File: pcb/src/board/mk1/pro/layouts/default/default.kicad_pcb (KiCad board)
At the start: 2 copper layers, 0 parts

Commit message: pcb: add MCU to Wonkleboard mk.1 Pro
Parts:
- added C1: 100nF ±10%, Samsung_Electro_Mechanics_CL05B104KO5NNNC:C0402, F.Cu at (20.0, 0.00)
- added C10: 100nF ±10%, Samsung_Electro_Mechanics_CL05B104KO5NNNC:C0402, F.Cu at (20.0, -90.0)
- added C11: 100nF ±10%, Samsung_Electro_Mechanics_CL05B104KO5NNNC:C0402, F.Cu at (20.0, -100.0)
- added C12: 100nF ±10%, Samsung_Electro_Mechanics_CL05B104KO5NNNC:C0402, F.Cu at (20.0, -110.0)
- added C13: 20pF ±5%, FH_0402CG200J500NT:C0402, F.Cu at (20.0, -130.0)
- added C14: 20pF ±5%, FH_0402CG200J500NT:C0402, F.Cu at (20.0, -140.0)
- added C15: 2.2µF ±20%, Samsung_Electro_Mechanics_CL05A225MQ5NSNC:C0402, F.Cu at (20.0, -150.0)
- added C16: 2.2µF ±20%, Samsung_Electro_Mechanics_CL05A225MQ5NSNC:C0402, F.Cu at (20.0, -160.0)
- added C17: 1µF ±10%, Samsung_Electro_Mechanics_CL05A105KA5NQNC:C0402, F.Cu at (20.0, -170.0)
- added C18: 100nF ±10%, Samsung_Electro_Mechanics_CL05B104KO5NNNC:C0402, F.Cu at (20.0, -180.0)
- added C2: 100nF ±10%, Samsung_Electro_Mechanics_CL05B104KO5NNNC:C0402, F.Cu at (20.0, -10.0)
- added C3: 100nF ±10%, Samsung_Electro_Mechanics_CL05B104KO5NNNC:C0402, F.Cu at (20.0, -20.0)
- added C4: 100nF ±10%, Samsung_Electro_Mechanics_CL05B104KO5NNNC:C0402, F.Cu at (20.0, -30.0)
- added C5: 100nF ±10%, Samsung_Electro_Mechanics_CL05B104KO5NNNC:C0402, F.Cu at (20.0, -40.0)
- added C6: 100nF ±10%, Samsung_Electro_Mechanics_CL05B104KO5NNNC:C0402, F.Cu at (20.0, -50.0)
- added C7: 100nF ±10%, Samsung_Electro_Mechanics_CL05B104KO5NNNC:C0402, F.Cu at (20.0, -60.0)
- added C8: 100nF ±10%, Samsung_Electro_Mechanics_CL05B104KO5NNNC:C0402, F.Cu at (20.0, -70.0)
- added C9: 100nF ±10%, Samsung_Electro_Mechanics_CL05B104KO5NNNC:C0402, F.Cu at (20.0, -80.0)
- added R1: 1kΩ ±1%, UNI_ROYAL_0402WGF1001TCE:R0402, F.Cu at (20.0, -120.0)
- added U1: , STMicroelectronics_STM32F429IGT6:LQFP-176_L24.0-W24.0-P0.50-LS26.0-BL, F.Cu at (0.00, 0.00)
- added X1: , TAE_TAXM8M4RFDCET2T:CRYSTAL-SMD_4P-L3.2-W2.5-BL-2, F.Cu at (10.0, 0.00)

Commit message: pcb: add MUX and sensors to Wonkleboard mk.1 Pro
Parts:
- added U10: , PJSEMI_AH49HSC:SOT-23-3_L2.9-W1.6-P1.90-LS2.8-BR, F.Cu at (72.0, 0.00)
- added U100: , PJSEMI_AH49HSC:SOT-23-3_L2.9-W1.6-P1.90-LS2.8-BR, F.Cu at (882.0, 0.00)
- added U101: , PJSEMI_AH49HSC:SOT-23-3_L2.9-W1.6-P1.90-LS2.8-BR, F.Cu at (891.0, 0.00)
- added U102: , PJSEMI_AH49HSC:SOT-23-3_L2.9-W1.6-P1.90-LS2.8-BR, F.Cu at (900.0, 0.00)
- added U103: , PJSEMI_AH49HSC:SOT-23-3_L2.9-W1.6-P1.90-LS2.8-BR, F.Cu at (909.0, 0.00)
- added U104: , PJSEMI_AH49HSC:SOT-23-3_L2.9-W1.6-P1.90-LS2.8-BR, F.Cu at (918.0, 0.00)
- added U105: , PJSEMI_AH49HSC:SOT-23-3_L2.9-W1.6-P1.90-LS2.8-BR, F.Cu at (927.0, 0.00)
- added U106: , PJSEMI_AH49HSC:SOT-23-3_L2.9-W1.6-P1.90-LS2.8-BR, F.Cu at (936.0, 0.00)
- added U107: , PJSEMI_AH49HSC:SOT-23-3_L2.9-W1.6-P1.90-LS2.8-BR, F.Cu at (945.0, 0.00)
- added U108: , PJSEMI_AH49HSC:SOT-23-3_L2.9-W1.6-P1.90-LS2.8-BR, F.Cu at (954.0, 0.00)
- added U109: , PJSEMI_AH49HSC:SOT-23-3_L2.9-W1.6-P1.90-LS2.8-BR, F.Cu at (963.0, 0.00)
- added U11: , PJSEMI_AH49HSC:SOT-23-3_L2.9-W1.6-P1.90-LS2.8-BR, F.Cu at (81.0, 0.00)
- added U110: , Texas_Instruments_CD74HC4067SM96:SSOP-24_L8.1-W5.3-P0.65-LS7.8-BL, F.Cu at (972.0, 0.00)
- added U111: , PJSEMI_AH49HSC:SOT-23-3_L2.9-W1.6-P1.90-LS2.8-BR, F.Cu at (981.0, 0.00)
- added U112: , PJSEMI_AH49HSC:SOT-23-3_L2.9-W1.6-P1.90-LS2.8-BR, F.Cu at (990.0, 0.00)
- added U113: , PJSEMI_AH49HSC:SOT-23-3_L2.9-W1.6-P1.90-LS2.8-BR, F.Cu at (999.0, 0.00)
- added U114: , PJSEMI_AH49HSC:SOT-23-3_L2.9-W1.6-P1.90-LS2.8-BR, F.Cu at (1008.0, 0.00)
- added U115: , PJSEMI_AH49HSC:SOT-23-3_L2.9-W1.6-P1.90-LS2.8-BR, F.Cu at (1017.0, 0.00)
- added U116: , PJSEMI_AH49HSC:SOT-23-3_L2.9-W1.6-P1.90-LS2.8-BR, F.Cu at (1026.0, 0.00)
- added U117: , PJSEMI_AH49HSC:SOT-23-3_L2.9-W1.6-P1.90-LS2.8-BR, F.Cu at (1035.0, 0.00)
- added U118: , PJSEMI_AH49HSC:SOT-23-3_L2.9-W1.6-P1.90-LS2.8-BR, F.Cu at (1044.0, 0.00)
- added U119: , PJSEMI_AH49HSC:SOT-23-3_L2.9-W1.6-P1.90-LS2.8-BR, F.Cu at (1053.0, 0.00)
- added U12: , PJSEMI_AH49HSC:SOT-23-3_L2.9-W1.6-P1.90-LS2.8-BR, F.Cu at (90.0, 0.00)
- added U120: , PJSEMI_AH49HSC:SOT-23-3_L2.9-W1.6-P1.90-LS2.8-BR, F.Cu at (1062.0, 0.00)
- added U121: , PJSEMI_AH49HSC:SOT-23-3_L2.9-W1.6-P1.90-LS2.8-BR, F.Cu at (1071.0, 0.00)
- added U122: , Texas_Instruments_CD74HC4067SM96:SSOP-24_L8.1-W5.3-P0.65-LS7.8-BL, F.Cu at (1080.0, 0.00)
- added U123: , PJSEMI_AH49HSC:SOT-23-3_L2.9-W1.6-P1.90-LS2.8-BR, F.Cu at (1089.0, 0.00)
- added U124: , PJSEMI_AH49HSC:SOT-23-3_L2.9-W1.6-P1.90-LS2.8-BR, F.Cu at (1098.0, 0.00)
- added U125: , PJSEMI_AH49HSC:SOT-23-3_L2.9-W1.6-P1.90-LS2.8-BR, F.Cu at (1107.0, 0.00)
- added U126: , PJSEMI_AH49HSC:SOT-23-3_L2.9-W1.6-P1.90-LS2.8-BR, F.Cu at (1116.0, 0.00)
- added U127: , PJSEMI_AH49HSC:SOT-23-3_L2.9-W1.6-P1.90-LS2.8-BR, F.Cu at (1125.0, 0.00)
- added U128: , PJSEMI_AH49HSC:SOT-23-3_L2.9-W1.6-P1.90-LS2.8-BR, F.Cu at (1134.0, 0.00)
- added U129: , PJSEMI_AH49HSC:SOT-23-3_L2.9-W1.6-P1.90-LS2.8-BR, F.Cu at (1143.0, 0.00)
- added U13: , PJSEMI_AH49HSC:SOT-23-3_L2.9-W1.6-P1.90-LS2.8-BR, F.Cu at (99.0, 0.00)
- added U130: , PJSEMI_AH49HSC:SOT-23-3_L2.9-W1.6-P1.90-LS2.8-BR, F.Cu at (1152.0, 0.00)
- added U131: , PJSEMI_AH49HSC:SOT-23-3_L2.9-W1.6-P1.90-LS2.8-BR, F.Cu at (1161.0, 0.00)
- added U132: , PJSEMI_AH49HSC:SOT-23-3_L2.9-W1.6-P1.90-LS2.8-BR, F.Cu at (1170.0, 0.00)
- added U133: , PJSEMI_AH49HSC:SOT-23-3_L2.9-W1.6-P1.90-LS2.8-BR, F.Cu at (1179.0, 0.00)
- added U134: , Texas_Instruments_CD74HC4067SM96:SSOP-24_L8.1-W5.3-P0.65-LS7.8-BL, F.Cu at (1188.0, 0.00)
- added U135: , PJSEMI_AH49HSC:SOT-23-3_L2.9-W1.6-P1.90-LS2.8-BR, F.Cu at (1197.0, 0.00)
- added U136: , PJSEMI_AH49HSC:SOT-23-3_L2.9-W1.6-P1.90-LS2.8-BR, F.Cu at (1206.0, 0.00)
- added U137: , PJSEMI_AH49HSC:SOT-23-3_L2.9-W1.6-P1.90-LS2.8-BR, F.Cu at (1215.0, 0.00)
- added U138: , PJSEMI_AH49HSC:SOT-23-3_L2.9-W1.6-P1.90-LS2.8-BR, F.Cu at (1224.0, 0.00)
- added U139: , PJSEMI_AH49HSC:SOT-23-3_L2.9-W1.6-P1.90-LS2.8-BR, F.Cu at (1233.0, 0.00)
- added U14: , Texas_Instruments_CD74HC4067SM96:SSOP-24_L8.1-W5.3-P0.65-LS7.8-BL, F.Cu at (108.0, 0.00)
- added U140: , PJSEMI_AH49HSC:SOT-23-3_L2.9-W1.6-P1.90-LS2.8-BR, F.Cu at (1242.0, 0.00)
- added U141: , PJSEMI_AH49HSC:SOT-23-3_L2.9-W1.6-P1.90-LS2.8-BR, F.Cu at (1251.0, 0.00)
- added U142: , PJSEMI_AH49HSC:SOT-23-3_L2.9-W1.6-P1.90-LS2.8-BR, F.Cu at (1260.0, 0.00)
- added U143: , PJSEMI_AH49HSC:SOT-23-3_L2.9-W1.6-P1.90-LS2.8-BR, F.Cu at (1269.0, 0.00)
- added U144: , PJSEMI_AH49HSC:SOT-23-3_L2.9-W1.6-P1.90-LS2.8-BR, F.Cu at (1278.0, 0.00)
- added U145: , PJSEMI_AH49HSC:SOT-23-3_L2.9-W1.6-P1.90-LS2.8-BR, F.Cu at (1287.0, 0.00)
- added U146: , Texas_Instruments_CD74HC4067SM96:SSOP-24_L8.1-W5.3-P0.65-LS7.8-BL, F.Cu at (1296.0, 0.00)
- added U147: , PJSEMI_AH49HSC:SOT-23-3_L2.9-W1.6-P1.90-LS2.8-BR, F.Cu at (1305.0, 0.00)
- added U148: , PJSEMI_AH49HSC:SOT-23-3_L2.9-W1.6-P1.90-LS2.8-BR, F.Cu at (1314.0, 0.00)
- added U149: , PJSEMI_AH49HSC:SOT-23-3_L2.9-W1.6-P1.90-LS2.8-BR, F.Cu at (1323.0, 0.00)
- added U15: , PJSEMI_AH49HSC:SOT-23-3_L2.9-W1.6-P1.90-LS2.8-BR, F.Cu at (117.0, 0.00)
- added U150: , PJSEMI_AH49HSC:SOT-23-3_L2.9-W1.6-P1.90-LS2.8-BR, F.Cu at (1332.0, 0.00)
- added U151: , PJSEMI_AH49HSC:SOT-23-3_L2.9-W1.6-P1.90-LS2.8-BR, F.Cu at (1341.0, 0.00)
- added U152: , PJSEMI_AH49HSC:SOT-23-3_L2.9-W1.6-P1.90-LS2.8-BR, F.Cu at (1350.0, 0.00)
- added U153: , PJSEMI_AH49HSC:SOT-23-3_L2.9-W1.6-P1.90-LS2.8-BR, F.Cu at (1359.0, 0.00)
- added U154: , PJSEMI_AH49HSC:SOT-23-3_L2.9-W1.6-P1.90-LS2.8-BR, F.Cu at (1368.0, 0.00)
- added U155: , PJSEMI_AH49HSC:SOT-23-3_L2.9-W1.6-P1.90-LS2.8-BR, F.Cu at (1377.0, 0.00)
- added U156: , PJSEMI_AH49HSC:SOT-23-3_L2.9-W1.6-P1.90-LS2.8-BR, F.Cu at (1386.0, 0.00)
- added U157: , PJSEMI_AH49HSC:SOT-23-3_L2.9-W1.6-P1.90-LS2.8-BR, F.Cu at (1395.0, 0.00)
- added U158: , Texas_Instruments_CD74HC4067SM96:SSOP-24_L8.1-W5.3-P0.65-LS7.8-BL, F.Cu at (1404.0, 0.00)
- added U159: , PJSEMI_AH49HSC:SOT-23-3_L2.9-W1.6-P1.90-LS2.8-BR, F.Cu at (1413.0, 0.00)
- added U16: , PJSEMI_AH49HSC:SOT-23-3_L2.9-W1.6-P1.90-LS2.8-BR, F.Cu at (126.0, 0.00)
- added U160: , PJSEMI_AH49HSC:SOT-23-3_L2.9-W1.6-P1.90-LS2.8-BR, F.Cu at (1422.0, 0.00)
- added U161: , PJSEMI_AH49HSC:SOT-23-3_L2.9-W1.6-P1.90-LS2.8-BR, F.Cu at (1431.0, 0.00)
- added U162: , PJSEMI_AH49HSC:SOT-23-3_L2.9-W1.6-P1.90-LS2.8-BR, F.Cu at (1440.0, 0.00)
- added U163: , PJSEMI_AH49HSC:SOT-23-3_L2.9-W1.6-P1.90-LS2.8-BR, F.Cu at (1449.0, 0.00)
- added U164: , PJSEMI_AH49HSC:SOT-23-3_L2.9-W1.6-P1.90-LS2.8-BR, F.Cu at (1458.0, 0.00)
- added U165: , PJSEMI_AH49HSC:SOT-23-3_L2.9-W1.6-P1.90-LS2.8-BR, F.Cu at (1467.0, 0.00)
- added U166: , PJSEMI_AH49HSC:SOT-23-3_L2.9-W1.6-P1.90-LS2.8-BR, F.Cu at (1476.0, 0.00)
- added U167: , PJSEMI_AH49HSC:SOT-23-3_L2.9-W1.6-P1.90-LS2.8-BR, F.Cu at (1485.0, 0.00)
- added U168: , PJSEMI_AH49HSC:SOT-23-3_L2.9-W1.6-P1.90-LS2.8-BR, F.Cu at (1494.0, 0.00)
- added U169: , PJSEMI_AH49HSC:SOT-23-3_L2.9-W1.6-P1.90-LS2.8-BR, F.Cu at (1503.0, 0.00)
- added U17: , PJSEMI_AH49HSC:SOT-23-3_L2.9-W1.6-P1.90-LS2.8-BR, F.Cu at (135.0, 0.00)
- added U170: , Texas_Instruments_CD74HC4067SM96:SSOP-24_L8.1-W5.3-P0.65-LS7.8-BL, F.Cu at (1512.0, 0.00)
- added U171: , PJSEMI_AH49HSC:SOT-23-3_L2.9-W1.6-P1.90-LS2.8-BR, F.Cu at (1521.0, 0.00)
- added U172: , PJSEMI_AH49HSC:SOT-23-3_L2.9-W1.6-P1.90-LS2.8-BR, F.Cu at (1530.0, 0.00)
- added U173: , PJSEMI_AH49HSC:SOT-23-3_L2.9-W1.6-P1.90-LS2.8-BR, F.Cu at (1539.0, 0.00)
- added U174: , PJSEMI_AH49HSC:SOT-23-3_L2.9-W1.6-P1.90-LS2.8-BR, F.Cu at (1548.0, 0.00)
- added U175: , PJSEMI_AH49HSC:SOT-23-3_L2.9-W1.6-P1.90-LS2.8-BR, F.Cu at (1557.0, 0.00)
- added U176: , PJSEMI_AH49HSC:SOT-23-3_L2.9-W1.6-P1.90-LS2.8-BR, F.Cu at (1566.0, 0.00)
- added U177: , PJSEMI_AH49HSC:SOT-23-3_L2.9-W1.6-P1.90-LS2.8-BR, F.Cu at (1575.0, 0.00)
- added U178: , PJSEMI_AH49HSC:SOT-23-3_L2.9-W1.6-P1.90-LS2.8-BR, F.Cu at (1584.0, 0.00)
- added U179: , PJSEMI_AH49HSC:SOT-23-3_L2.9-W1.6-P1.90-LS2.8-BR, F.Cu at (1593.0, 0.00)
- added U18: , PJSEMI_AH49HSC:SOT-23-3_L2.9-W1.6-P1.90-LS2.8-BR, F.Cu at (144.0, 0.00)
- added U180: , PJSEMI_AH49HSC:SOT-23-3_L2.9-W1.6-P1.90-LS2.8-BR, F.Cu at (1602.0, 0.00)
- added U181: , PJSEMI_AH49HSC:SOT-23-3_L2.9-W1.6-P1.90-LS2.8-BR, F.Cu at (1611.0, 0.00)
- added U182: , Texas_Instruments_CD74HC4067SM96:SSOP-24_L8.1-W5.3-P0.65-LS7.8-BL, F.Cu at (1620.0, 0.00)
- added U183: , PJSEMI_AH49HSC:SOT-23-3_L2.9-W1.6-P1.90-LS2.8-BR, F.Cu at (1629.0, 0.00)
- added U184: , PJSEMI_AH49HSC:SOT-23-3_L2.9-W1.6-P1.90-LS2.8-BR, F.Cu at (1638.0, 0.00)
- added U185: , PJSEMI_AH49HSC:SOT-23-3_L2.9-W1.6-P1.90-LS2.8-BR, F.Cu at (1647.0, 0.00)
- added U186: , PJSEMI_AH49HSC:SOT-23-3_L2.9-W1.6-P1.90-LS2.8-BR, F.Cu at (1656.0, 0.00)
- added U187: , PJSEMI_AH49HSC:SOT-23-3_L2.9-W1.6-P1.90-LS2.8-BR, F.Cu at (1665.0, 0.00)
- added U188: , PJSEMI_AH49HSC:SOT-23-3_L2.9-W1.6-P1.90-LS2.8-BR, F.Cu at (1674.0, 0.00)
- added U189: , PJSEMI_AH49HSC:SOT-23-3_L2.9-W1.6-P1.90-LS2.8-BR, F.Cu at (1683.0, 0.00)
- added U19: , PJSEMI_AH49HSC:SOT-23-3_L2.9-W1.6-P1.90-LS2.8-BR, F.Cu at (153.0, 0.00)
- added U190: , PJSEMI_AH49HSC:SOT-23-3_L2.9-W1.6-P1.90-LS2.8-BR, F.Cu at (1692.0, 0.00)
- added U191: , PJSEMI_AH49HSC:SOT-23-3_L2.9-W1.6-P1.90-LS2.8-BR, F.Cu at (1701.0, 0.00)
- added U192: , PJSEMI_AH49HSC:SOT-23-3_L2.9-W1.6-P1.90-LS2.8-BR, F.Cu at (1710.0, 0.00)
- added U193: , PJSEMI_AH49HSC:SOT-23-3_L2.9-W1.6-P1.90-LS2.8-BR, F.Cu at (1719.0, 0.00)
- added U194: , Texas_Instruments_CD74HC4067SM96:SSOP-24_L8.1-W5.3-P0.65-LS7.8-BL, F.Cu at (1728.0, 0.00)
- added U195: , PJSEMI_AH49HSC:SOT-23-3_L2.9-W1.6-P1.90-LS2.8-BR, F.Cu at (1737.0, 0.00)
- added U196: , PJSEMI_AH49HSC:SOT-23-3_L2.9-W1.6-P1.90-LS2.8-BR, F.Cu at (1746.0, 0.00)
- added U197: , PJSEMI_AH49HSC:SOT-23-3_L2.9-W1.6-P1.90-LS2.8-BR, F.Cu at (1755.0, 0.00)
- added U198: , PJSEMI_AH49HSC:SOT-23-3_L2.9-W1.6-P1.90-LS2.8-BR, F.Cu at (1764.0, 0.00)
- added U199: , PJSEMI_AH49HSC:SOT-23-3_L2.9-W1.6-P1.90-LS2.8-BR, F.Cu at (1773.0, 0.00)
- added U2: , Texas_Instruments_CD74HC4067SM96:SSOP-24_L8.1-W5.3-P0.65-LS7.8-BL, F.Cu at (0.00, 0.00)
- added U20: , PJSEMI_AH49HSC:SOT-23-3_L2.9-W1.6-P1.90-LS2.8-BR, F.Cu at (162.0, 0.00)
- added U200: , PJSEMI_AH49HSC:SOT-23-3_L2.9-W1.6-P1.90-LS2.8-BR, F.Cu at (1782.0, 0.00)
- added U201: , PJSEMI_AH49HSC:SOT-23-3_L2.9-W1.6-P1.90-LS2.8-BR, F.Cu at (1791.0, 0.00)
- added U202: , PJSEMI_AH49HSC:SOT-23-3_L2.9-W1.6-P1.90-LS2.8-BR, F.Cu at (1800.0, 0.00)
- added U203: , PJSEMI_AH49HSC:SOT-23-3_L2.9-W1.6-P1.90-LS2.8-BR, F.Cu at (1809.0, 0.00)
- added U204: , PJSEMI_AH49HSC:SOT-23-3_L2.9-W1.6-P1.90-LS2.8-BR, F.Cu at (1818.0, 0.00)
- added U205: , PJSEMI_AH49HSC:SOT-23-3_L2.9-W1.6-P1.90-LS2.8-BR, F.Cu at (1827.0, 0.00)
- added U206: , Texas_Instruments_CD74HC4067SM96:SSOP-24_L8.1-W5.3-P0.65-LS7.8-BL, F.Cu at (1836.0, 0.00)
- added U207: , PJSEMI_AH49HSC:SOT-23-3_L2.9-W1.6-P1.90-LS2.8-BR, F.Cu at (1845.0, 0.00)
- added U208: , PJSEMI_AH49HSC:SOT-23-3_L2.9-W1.6-P1.90-LS2.8-BR, F.Cu at (1854.0, 0.00)
- added U209: , PJSEMI_AH49HSC:SOT-23-3_L2.9-W1.6-P1.90-LS2.8-BR, F.Cu at (1863.0, 0.00)
- added U21: , PJSEMI_AH49HSC:SOT-23-3_L2.9-W1.6-P1.90-LS2.8-BR, F.Cu at (171.0, 0.00)
- added U210: , PJSEMI_AH49HSC:SOT-23-3_L2.9-W1.6-P1.90-LS2.8-BR, F.Cu at (1872.0, 0.00)
- added U211: , PJSEMI_AH49HSC:SOT-23-3_L2.9-W1.6-P1.90-LS2.8-BR, F.Cu at (1881.0, 0.00)
- added U212: , PJSEMI_AH49HSC:SOT-23-3_L2.9-W1.6-P1.90-LS2.8-BR, F.Cu at (1890.0, 0.00)
- added U213: , PJSEMI_AH49HSC:SOT-23-3_L2.9-W1.6-P1.90-LS2.8-BR, F.Cu at (1899.0, 0.00)
- added U214: , PJSEMI_AH49HSC:SOT-23-3_L2.9-W1.6-P1.90-LS2.8-BR, F.Cu at (1908.0, 0.00)
- added U215: , PJSEMI_AH49HSC:SOT-23-3_L2.9-W1.6-P1.90-LS2.8-BR, F.Cu at (1917.0, 0.00)
- added U216: , PJSEMI_AH49HSC:SOT-23-3_L2.9-W1.6-P1.90-LS2.8-BR, F.Cu at (1926.0, 0.00)
- added U217: , PJSEMI_AH49HSC:SOT-23-3_L2.9-W1.6-P1.90-LS2.8-BR, F.Cu at (1935.0, 0.00)
- added U218: , Texas_Instruments_CD74HC4067SM96:SSOP-24_L8.1-W5.3-P0.65-LS7.8-BL, F.Cu at (1944.0, 0.00)
- added U219: , PJSEMI_AH49HSC:SOT-23-3_L2.9-W1.6-P1.90-LS2.8-BR, F.Cu at (1953.0, 0.00)
- added U22: , PJSEMI_AH49HSC:SOT-23-3_L2.9-W1.6-P1.90-LS2.8-BR, F.Cu at (180.0, 0.00)
- added U220: , PJSEMI_AH49HSC:SOT-23-3_L2.9-W1.6-P1.90-LS2.8-BR, F.Cu at (1962.0, 0.00)
- added U221: , PJSEMI_AH49HSC:SOT-23-3_L2.9-W1.6-P1.90-LS2.8-BR, F.Cu at (1971.0, 0.00)
- added U222: , PJSEMI_AH49HSC:SOT-23-3_L2.9-W1.6-P1.90-LS2.8-BR, F.Cu at (1980.0, 0.00)
- added U223: , PJSEMI_AH49HSC:SOT-23-3_L2.9-W1.6-P1.90-LS2.8-BR, F.Cu at (1989.0, 0.00)
- added U224: , PJSEMI_AH49HSC:SOT-23-3_L2.9-W1.6-P1.90-LS2.8-BR, F.Cu at (1998.0, 0.00)
- added U225: , PJSEMI_AH49HSC:SOT-23-3_L2.9-W1.6-P1.90-LS2.8-BR, F.Cu at (2007.0, 0.00)
- added U226: , PJSEMI_AH49HSC:SOT-23-3_L2.9-W1.6-P1.90-LS2.8-BR, F.Cu at (2016.0, 0.00)
- added U227: , PJSEMI_AH49HSC:SOT-23-3_L2.9-W1.6-P1.90-LS2.8-BR, F.Cu at (2025.0, 0.00)
- added U228: , PJSEMI_AH49HSC:SOT-23-3_L2.9-W1.6-P1.90-LS2.8-BR, F.Cu at (2034.0, 0.00)
- added U229: , PJSEMI_AH49HSC:SOT-23-3_L2.9-W1.6-P1.90-LS2.8-BR, F.Cu at (2043.0, 0.00)
- added U23: , PJSEMI_AH49HSC:SOT-23-3_L2.9-W1.6-P1.90-LS2.8-BR, F.Cu at (189.0, 0.00)
- added U24: , PJSEMI_AH49HSC:SOT-23-3_L2.9-W1.6-P1.90-LS2.8-BR, F.Cu at (198.0, 0.00)
- added U25: , PJSEMI_AH49HSC:SOT-23-3_L2.9-W1.6-P1.90-LS2.8-BR, F.Cu at (207.0, 0.00)
- added U26: , Texas_Instruments_CD74HC4067SM96:SSOP-24_L8.1-W5.3-P0.65-LS7.8-BL, F.Cu at (216.0, 0.00)
- added U27: , PJSEMI_AH49HSC:SOT-23-3_L2.9-W1.6-P1.90-LS2.8-BR, F.Cu at (225.0, 0.00)
- added U28: , PJSEMI_AH49HSC:SOT-23-3_L2.9-W1.6-P1.90-LS2.8-BR, F.Cu at (234.0, 0.00)
- added U29: , PJSEMI_AH49HSC:SOT-23-3_L2.9-W1.6-P1.90-LS2.8-BR, F.Cu at (243.0, 0.00)
- added U3: , PJSEMI_AH49HSC:SOT-23-3_L2.9-W1.6-P1.90-LS2.8-BR, F.Cu at (9.00, 0.00)
- added U30: , PJSEMI_AH49HSC:SOT-23-3_L2.9-W1.6-P1.90-LS2.8-BR, F.Cu at (252.0, 0.00)
- added U31: , PJSEMI_AH49HSC:SOT-23-3_L2.9-W1.6-P1.90-LS2.8-BR, F.Cu at (261.0, 0.00)
- added U32: , PJSEMI_AH49HSC:SOT-23-3_L2.9-W1.6-P1.90-LS2.8-BR, F.Cu at (270.0, 0.00)
- added U33: , PJSEMI_AH49HSC:SOT-23-3_L2.9-W1.6-P1.90-LS2.8-BR, F.Cu at (279.0, 0.00)
- added U34: , PJSEMI_AH49HSC:SOT-23-3_L2.9-W1.6-P1.90-LS2.8-BR, F.Cu at (288.0, 0.00)
- added U35: , PJSEMI_AH49HSC:SOT-23-3_L2.9-W1.6-P1.90-LS2.8-BR, F.Cu at (297.0, 0.00)
- added U36: , PJSEMI_AH49HSC:SOT-23-3_L2.9-W1.6-P1.90-LS2.8-BR, F.Cu at (306.0, 0.00)
- added U37: , PJSEMI_AH49HSC:SOT-23-3_L2.9-W1.6-P1.90-LS2.8-BR, F.Cu at (315.0, 0.00)
- added U38: , Texas_Instruments_CD74HC4067SM96:SSOP-24_L8.1-W5.3-P0.65-LS7.8-BL, F.Cu at (324.0, 0.00)
- added U39: , PJSEMI_AH49HSC:SOT-23-3_L2.9-W1.6-P1.90-LS2.8-BR, F.Cu at (333.0, 0.00)
- added U4: , PJSEMI_AH49HSC:SOT-23-3_L2.9-W1.6-P1.90-LS2.8-BR, F.Cu at (18.0, 0.00)
- added U40: , PJSEMI_AH49HSC:SOT-23-3_L2.9-W1.6-P1.90-LS2.8-BR, F.Cu at (342.0, 0.00)
- added U41: , PJSEMI_AH49HSC:SOT-23-3_L2.9-W1.6-P1.90-LS2.8-BR, F.Cu at (351.0, 0.00)
- added U42: , PJSEMI_AH49HSC:SOT-23-3_L2.9-W1.6-P1.90-LS2.8-BR, F.Cu at (360.0, 0.00)
- added U43: , PJSEMI_AH49HSC:SOT-23-3_L2.9-W1.6-P1.90-LS2.8-BR, F.Cu at (369.0, 0.00)
- added U44: , PJSEMI_AH49HSC:SOT-23-3_L2.9-W1.6-P1.90-LS2.8-BR, F.Cu at (378.0, 0.00)
- added U45: , PJSEMI_AH49HSC:SOT-23-3_L2.9-W1.6-P1.90-LS2.8-BR, F.Cu at (387.0, 0.00)
- added U46: , PJSEMI_AH49HSC:SOT-23-3_L2.9-W1.6-P1.90-LS2.8-BR, F.Cu at (396.0, 0.00)
- added U47: , PJSEMI_AH49HSC:SOT-23-3_L2.9-W1.6-P1.90-LS2.8-BR, F.Cu at (405.0, 0.00)
- added U48: , PJSEMI_AH49HSC:SOT-23-3_L2.9-W1.6-P1.90-LS2.8-BR, F.Cu at (414.0, 0.00)
- added U49: , PJSEMI_AH49HSC:SOT-23-3_L2.9-W1.6-P1.90-LS2.8-BR, F.Cu at (423.0, 0.00)
- added U5: , PJSEMI_AH49HSC:SOT-23-3_L2.9-W1.6-P1.90-LS2.8-BR, F.Cu at (27.0, 0.00)
- added U50: , Texas_Instruments_CD74HC4067SM96:SSOP-24_L8.1-W5.3-P0.65-LS7.8-BL, F.Cu at (432.0, 0.00)
- added U51: , PJSEMI_AH49HSC:SOT-23-3_L2.9-W1.6-P1.90-LS2.8-BR, F.Cu at (441.0, 0.00)
- added U52: , PJSEMI_AH49HSC:SOT-23-3_L2.9-W1.6-P1.90-LS2.8-BR, F.Cu at (450.0, 0.00)
- added U53: , PJSEMI_AH49HSC:SOT-23-3_L2.9-W1.6-P1.90-LS2.8-BR, F.Cu at (459.0, 0.00)
- added U54: , PJSEMI_AH49HSC:SOT-23-3_L2.9-W1.6-P1.90-LS2.8-BR, F.Cu at (468.0, 0.00)
- added U55: , PJSEMI_AH49HSC:SOT-23-3_L2.9-W1.6-P1.90-LS2.8-BR, F.Cu at (477.0, 0.00)
- added U56: , PJSEMI_AH49HSC:SOT-23-3_L2.9-W1.6-P1.90-LS2.8-BR, F.Cu at (486.0, 0.00)
- added U57: , PJSEMI_AH49HSC:SOT-23-3_L2.9-W1.6-P1.90-LS2.8-BR, F.Cu at (495.0, 0.00)
- added U58: , PJSEMI_AH49HSC:SOT-23-3_L2.9-W1.6-P1.90-LS2.8-BR, F.Cu at (504.0, 0.00)
- added U59: , PJSEMI_AH49HSC:SOT-23-3_L2.9-W1.6-P1.90-LS2.8-BR, F.Cu at (513.0, 0.00)
- added U6: , PJSEMI_AH49HSC:SOT-23-3_L2.9-W1.6-P1.90-LS2.8-BR, F.Cu at (36.0, 0.00)
- added U60: , PJSEMI_AH49HSC:SOT-23-3_L2.9-W1.6-P1.90-LS2.8-BR, F.Cu at (522.0, 0.00)
- added U61: , PJSEMI_AH49HSC:SOT-23-3_L2.9-W1.6-P1.90-LS2.8-BR, F.Cu at (531.0, 0.00)
- added U62: , Texas_Instruments_CD74HC4067SM96:SSOP-24_L8.1-W5.3-P0.65-LS7.8-BL, F.Cu at (540.0, 0.00)
- added U63: , PJSEMI_AH49HSC:SOT-23-3_L2.9-W1.6-P1.90-LS2.8-BR, F.Cu at (549.0, 0.00)
- added U64: , PJSEMI_AH49HSC:SOT-23-3_L2.9-W1.6-P1.90-LS2.8-BR, F.Cu at (558.0, 0.00)
- added U65: , PJSEMI_AH49HSC:SOT-23-3_L2.9-W1.6-P1.90-LS2.8-BR, F.Cu at (567.0, 0.00)
- added U66: , PJSEMI_AH49HSC:SOT-23-3_L2.9-W1.6-P1.90-LS2.8-BR, F.Cu at (576.0, 0.00)
- added U67: , PJSEMI_AH49HSC:SOT-23-3_L2.9-W1.6-P1.90-LS2.8-BR, F.Cu at (585.0, 0.00)
- added U68: , PJSEMI_AH49HSC:SOT-23-3_L2.9-W1.6-P1.90-LS2.8-BR, F.Cu at (594.0, 0.00)
- added U69: , PJSEMI_AH49HSC:SOT-23-3_L2.9-W1.6-P1.90-LS2.8-BR, F.Cu at (603.0, 0.00)
- added U7: , PJSEMI_AH49HSC:SOT-23-3_L2.9-W1.6-P1.90-LS2.8-BR, F.Cu at (45.0, 0.00)
- added U70: , PJSEMI_AH49HSC:SOT-23-3_L2.9-W1.6-P1.90-LS2.8-BR, F.Cu at (612.0, 0.00)
- added U71: , PJSEMI_AH49HSC:SOT-23-3_L2.9-W1.6-P1.90-LS2.8-BR, F.Cu at (621.0, 0.00)
- added U72: , PJSEMI_AH49HSC:SOT-23-3_L2.9-W1.6-P1.90-LS2.8-BR, F.Cu at (630.0, 0.00)
- added U73: , PJSEMI_AH49HSC:SOT-23-3_L2.9-W1.6-P1.90-LS2.8-BR, F.Cu at (639.0, 0.00)
- added U74: , Texas_Instruments_CD74HC4067SM96:SSOP-24_L8.1-W5.3-P0.65-LS7.8-BL, F.Cu at (648.0, 0.00)
- added U75: , PJSEMI_AH49HSC:SOT-23-3_L2.9-W1.6-P1.90-LS2.8-BR, F.Cu at (657.0, 0.00)
- added U76: , PJSEMI_AH49HSC:SOT-23-3_L2.9-W1.6-P1.90-LS2.8-BR, F.Cu at (666.0, 0.00)
- added U77: , PJSEMI_AH49HSC:SOT-23-3_L2.9-W1.6-P1.90-LS2.8-BR, F.Cu at (675.0, 0.00)
- added U78: , PJSEMI_AH49HSC:SOT-23-3_L2.9-W1.6-P1.90-LS2.8-BR, F.Cu at (684.0, 0.00)
- added U79: , PJSEMI_AH49HSC:SOT-23-3_L2.9-W1.6-P1.90-LS2.8-BR, F.Cu at (693.0, 0.00)
- added U8: , PJSEMI_AH49HSC:SOT-23-3_L2.9-W1.6-P1.90-LS2.8-BR, F.Cu at (54.0, 0.00)
- added U80: , PJSEMI_AH49HSC:SOT-23-3_L2.9-W1.6-P1.90-LS2.8-BR, F.Cu at (702.0, 0.00)
- added U81: , PJSEMI_AH49HSC:SOT-23-3_L2.9-W1.6-P1.90-LS2.8-BR, F.Cu at (711.0, 0.00)
- added U82: , PJSEMI_AH49HSC:SOT-23-3_L2.9-W1.6-P1.90-LS2.8-BR, F.Cu at (720.0, 0.00)
- added U83: , PJSEMI_AH49HSC:SOT-23-3_L2.9-W1.6-P1.90-LS2.8-BR, F.Cu at (729.0, 0.00)
- added U84: , PJSEMI_AH49HSC:SOT-23-3_L2.9-W1.6-P1.90-LS2.8-BR, F.Cu at (738.0, 0.00)
- added U85: , PJSEMI_AH49HSC:SOT-23-3_L2.9-W1.6-P1.90-LS2.8-BR, F.Cu at (747.0, 0.00)
- added U86: , Texas_Instruments_CD74HC4067SM96:SSOP-24_L8.1-W5.3-P0.65-LS7.8-BL, F.Cu at (756.0, 0.00)
- added U87: , PJSEMI_AH49HSC:SOT-23-3_L2.9-W1.6-P1.90-LS2.8-BR, F.Cu at (765.0, 0.00)
- added U88: , PJSEMI_AH49HSC:SOT-23-3_L2.9-W1.6-P1.90-LS2.8-BR, F.Cu at (774.0, 0.00)
- added U89: , PJSEMI_AH49HSC:SOT-23-3_L2.9-W1.6-P1.90-LS2.8-BR, F.Cu at (783.0, 0.00)
- added U9: , PJSEMI_AH49HSC:SOT-23-3_L2.9-W1.6-P1.90-LS2.8-BR, F.Cu at (63.0, 0.00)
- added U90: , PJSEMI_AH49HSC:SOT-23-3_L2.9-W1.6-P1.90-LS2.8-BR, F.Cu at (792.0, 0.00)
- added U91: , PJSEMI_AH49HSC:SOT-23-3_L2.9-W1.6-P1.90-LS2.8-BR, F.Cu at (801.0, 0.00)
- added U92: , PJSEMI_AH49HSC:SOT-23-3_L2.9-W1.6-P1.90-LS2.8-BR, F.Cu at (810.0, 0.00)
- added U93: , PJSEMI_AH49HSC:SOT-23-3_L2.9-W1.6-P1.90-LS2.8-BR, F.Cu at (819.0, 0.00)
- added U94: , PJSEMI_AH49HSC:SOT-23-3_L2.9-W1.6-P1.90-LS2.8-BR, F.Cu at (828.0, 0.00)
- added U95: , PJSEMI_AH49HSC:SOT-23-3_L2.9-W1.6-P1.90-LS2.8-BR, F.Cu at (837.0, 0.00)
- added U96: , PJSEMI_AH49HSC:SOT-23-3_L2.9-W1.6-P1.90-LS2.8-BR, F.Cu at (846.0, 0.00)
- added U97: , PJSEMI_AH49HSC:SOT-23-3_L2.9-W1.6-P1.90-LS2.8-BR, F.Cu at (855.0, 0.00)
- added U98: , Texas_Instruments_CD74HC4067SM96:SSOP-24_L8.1-W5.3-P0.65-LS7.8-BL, F.Cu at (864.0, 0.00)
- added U99: , PJSEMI_AH49HSC:SOT-23-3_L2.9-W1.6-P1.90-LS2.8-BR, F.Cu at (873.0, 0.00)
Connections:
- C1 pad 2: lv -> (no net)
- C10 pad 2: lv -> (no net)
- C11 pad 2: lv -> (no net)
- C12 pad 2: lv -> (no net)
- C13 pad 2: lv -> (no net)
- C14 pad 2: lv -> (no net)
- C15 pad 2: lv -> (no net)
- C16 pad 2: lv -> (no net)
- C17 pad 2: lv -> (no net)
- C18 pad 2: lv -> (no net)
- C2 pad 2: lv -> (no net)
- C3 pad 2: lv -> (no net)
- C4 pad 2: lv -> (no net)
- C5 pad 2: lv -> (no net)
- C6 pad 2: lv -> (no net)
- C7 pad 2: lv -> (no net)
- C8 pad 2: lv -> (no net)
- C9 pad 2: lv -> (no net)
- U1 pad 102: lv -> (no net)
- U1 pad 113: lv -> (no net)
- U1 pad 126: lv -> (no net)
- U1 pad 135: lv -> (no net)
- U1 pad 14: lv -> (no net)
- U1 pad 148: lv -> (no net)
- U1 pad 158: lv -> (no net)
- U1 pad 19: 19 -> gpio_f[3]-OUT
- U1 pad 2: 2 -> S3
- U1 pad 20: 20 -> gpio_f[4]-OUT
- U1 pad 21: 21 -> gpio_f[5]-OUT
- U1 pad 22: lv -> (no net)
- U1 pad 24: 24 -> gpio_f[6]-OUT
- U1 pad 25: 25 -> gpio_f[7]-OUT
- U1 pad 26: 26 -> gpio_f[8]-OUT
- U1 pad 27: 27 -> gpio_f[9]-OUT
- U1 pad 28: 28 -> gpio_f[10]-OUT
- U1 pad 3: 3 -> S2
- U1 pad 34: 34 -> gpio_c[2]-OUT
- U1 pad 35: 35 -> gpio_c[3]-OUT
- U1 pad 37: lv -> (no net)
- U1 pad 4: 4 -> S1
- U1 pad 41: 41 -> OUT
- U1 pad 42: 42 -> gpio_a[2]-OUT
- U1 pad 47: 47 -> gpio_a[3]-OUT
- U1 pad 5: 5 -> S0
- U1 pad 50: 50 -> gpio_a[4]-OUT
- U1 pad 52: 52 -> gpio_a[6]-OUT
- U1 pad 53: 53 -> gpio_a[7]-OUT
- U1 pad 54: 54 -> gpio_c[4]-OUT
- U1 pad 55: 55 -> gpio_c[5]-OUT
- U1 pad 61: lv -> (no net)
- U1 pad 71: lv -> (no net)
- U1 pad 90: lv -> (no net)
- X1 pad 2: lv -> (no net)
- X1 pad 4: lv -> (no net)

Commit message: pcb: oops forgot to commit this
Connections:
- C1 pad 2: (no net) -> lv
- C10 pad 2: (no net) -> lv
- C11 pad 2: (no net) -> lv
- C12 pad 2: (no net) -> lv
- C13 pad 2: (no net) -> lv
- C14 pad 2: (no net) -> lv
- C15 pad 2: (no net) -> lv
- C16 pad 2: (no net) -> lv
- C17 pad 2: (no net) -> lv
- C18 pad 2: (no net) -> lv
- C2 pad 2: (no net) -> lv
- C3 pad 2: (no net) -> lv
- C4 pad 2: (no net) -> lv
- C5 pad 2: (no net) -> lv
- C6 pad 2: (no net) -> lv
- C7 pad 2: (no net) -> lv
- C8 pad 2: (no net) -> lv
- C9 pad 2: (no net) -> lv
- U1 pad 102: (no net) -> lv
- U1 pad 113: (no net) -> lv
- U1 pad 126: (no net) -> lv
- U1 pad 135: (no net) -> lv
- U1 pad 14: (no net) -> lv
- U1 pad 148: (no net) -> lv
- U1 pad 158: (no net) -> lv
- U1 pad 22: (no net) -> lv
- U1 pad 37: (no net) -> lv
- U1 pad 61: (no net) -> lv
- U1 pad 71: (no net) -> lv
- U1 pad 90: (no net) -> lv
- U10 pad 3: (no net) -> lv
- U100 pad 3: (no net) -> lv
- U101 pad 3: (no net) -> lv
- U102 pad 3: (no net) -> lv
- U103 pad 3: (no net) -> lv
- U104 pad 3: (no net) -> lv
- U105 pad 3: (no net) -> lv
- U106 pad 3: (no net) -> lv
- U107 pad 3: (no net) -> lv
- U108 pad 3: (no net) -> lv
- U109 pad 3: (no net) -> lv
- U11 pad 3: (no net) -> lv
- U110 pad 12: (no net) -> lv
- U110 pad 15: (no net) -> lv
- U110 pad 16: (no net) -> lv
- U110 pad 17: (no net) -> lv
- U110 pad 18: (no net) -> lv
- U110 pad 19: (no net) -> lv
- U110 pad 20: (no net) -> lv
- U111 pad 3: (no net) -> lv
- U112 pad 3: (no net) -> lv
- U113 pad 3: (no net) -> lv
- U114 pad 3: (no net) -> lv
- U115 pad 3: (no net) -> lv
- U116 pad 3: (no net) -> lv
- U117 pad 3: (no net) -> lv
- U118 pad 3: (no net) -> lv
- U119 pad 3: (no net) -> lv
- U12 pad 3: (no net) -> lv
- U120 pad 3: (no net) -> lv
- U121 pad 3: (no net) -> lv
- U122 pad 12: (no net) -> lv
- U122 pad 15: (no net) -> lv
- U122 pad 16: (no net) -> lv
- U122 pad 17: (no net) -> lv
- U122 pad 18: (no net) -> lv
- U122 pad 19: (no net) -> lv
- U122 pad 20: (no net) -> lv
- U123 pad 3: (no net) -> lv
- U124 pad 3: (no net) -> lv
- U125 pad 3: (no net) -> lv
- U126 pad 3: (no net) -> lv
- U127 pad 3: (no net) -> lv
- U128 pad 3: (no net) -> lv
- U129 pad 3: (no net) -> lv
- U13 pad 3: (no net) -> lv
- U130 pad 3: (no net) -> lv
- U131 pad 3: (no net) -> lv
- U132 pad 3: (no net) -> lv
- U133 pad 3: (no net) -> lv
- U134 pad 12: (no net) -> lv
- U134 pad 15: (no net) -> lv
- U134 pad 16: (no net) -> lv
- U134 pad 17: (no net) -> lv
- U134 pad 18: (no net) -> lv
- U134 pad 19: (no net) -> lv
- U134 pad 20: (no net) -> lv
- U135 pad 3: (no net) -> lv
- U136 pad 3: (no net) -> lv
- U137 pad 3: (no net) -> lv
- U138 pad 3: (no net) -> lv
- U139 pad 3: (no net) -> lv
- U14 pad 12: (no net) -> lv
- U14 pad 15: (no net) -> lv
- U14 pad 16: (no net) -> lv
- U14 pad 17: (no net) -> lv
- U14 pad 18: (no net) -> lv
- U14 pad 19: (no net) -> lv
- U14 pad 20: (no net) -> lv
- U140 pad 3: (no net) -> lv
- U141 pad 3: (no net) -> lv
- U142 pad 3: (no net) -> lv
- U143 pad 3: (no net) -> lv
- U144 pad 3: (no net) -> lv
- U145 pad 3: (no net) -> lv
- U146 pad 12: (no net) -> lv
- U146 pad 15: (no net) -> lv
- U146 pad 16: (no net) -> lv
- U146 pad 17: (no net) -> lv
- U146 pad 18: (no net) -> lv
- U146 pad 19: (no net) -> lv
- U146 pad 20: (no net) -> lv
- U147 pad 3: (no net) -> lv
- U148 pad 3: (no net) -> lv
- U149 pad 3: (no net) -> lv
- U15 pad 3: (no net) -> lv
- U150 pad 3: (no net) -> lv
- U151 pad 3: (no net) -> lv
- U152 pad 3: (no net) -> lv
- U153 pad 3: (no net) -> lv
- U154 pad 3: (no net) -> lv
- U155 pad 3: (no net) -> lv
- U156 pad 3: (no net) -> lv
- U157 pad 3: (no net) -> lv
- U158 pad 12: (no net) -> lv
- U158 pad 15: (no net) -> lv
- U158 pad 16: (no net) -> lv
- U158 pad 17: (no net) -> lv
- U158 pad 18: (no net) -> lv
- U158 pad 19: (no net) -> lv
- U158 pad 20: (no net) -> lv
- U159 pad 3: (no net) -> lv
- U16 pad 3: (no net) -> lv
- U160 pad 3: (no net) -> lv
- U161 pad 3: (no net) -> lv
- U162 pad 3: (no net) -> lv
- U163 pad 3: (no net) -> lv
- U164 pad 3: (no net) -> lv
- U165 pad 3: (no net) -> lv
- U166 pad 3: (no net) -> lv
- U167 pad 3: (no net) -> lv
- U168 pad 3: (no net) -> lv
- U169 pad 3: (no net) -> lv
- U17 pad 3: (no net) -> lv
- U170 pad 12: (no net) -> lv
- U170 pad 15: (no net) -> lv
- U170 pad 16: (no net) -> lv
- U170 pad 17: (no net) -> lv
- U170 pad 18: (no net) -> lv
- U170 pad 19: (no net) -> lv
- U170 pad 20: (no net) -> lv
- U171 pad 3: (no net) -> lv
- U172 pad 3: (no net) -> lv
- U173 pad 3: (no net) -> lv
- U174 pad 3: (no net) -> lv
- U175 pad 3: (no net) -> lv
- U176 pad 3: (no net) -> lv
- U177 pad 3: (no net) -> lv
- U178 pad 3: (no net) -> lv
- U179 pad 3: (no net) -> lv
- U18 pad 3: (no net) -> lv
- U180 pad 3: (no net) -> lv
- U181 pad 3: (no net) -> lv
- U182 pad 12: (no net) -> lv
- U182 pad 15: (no net) -> lv
- U182 pad 16: (no net) -> lv
- U182 pad 17: (no net) -> lv
- U182 pad 18: (no net) -> lv
- U182 pad 19: (no net) -> lv
- U182 pad 20: (no net) -> lv
- U183 pad 3: (no net) -> lv
- U184 pad 3: (no net) -> lv
- U185 pad 3: (no net) -> lv
- U186 pad 3: (no net) -> lv
- U187 pad 3: (no net) -> lv
- U188 pad 3: (no net) -> lv
- U189 pad 3: (no net) -> lv
- U19 pad 3: (no net) -> lv
- U190 pad 3: (no net) -> lv
- U191 pad 3: (no net) -> lv
- U192 pad 3: (no net) -> lv
- U193 pad 3: (no net) -> lv
- U194 pad 12: (no net) -> lv
- U194 pad 15: (no net) -> lv
- U194 pad 16: (no net) -> lv
- U194 pad 17: (no net) -> lv
- U194 pad 18: (no net) -> lv
- U194 pad 19: (no net) -> lv
- U194 pad 20: (no net) -> lv
- U195 pad 3: (no net) -> lv
- U196 pad 3: (no net) -> lv
- U197 pad 3: (no net) -> lv
- U198 pad 3: (no net) -> lv
- U199 pad 3: (no net) -> lv
- U2 pad 12: (no net) -> lv
- U2 pad 15: (no net) -> lv
- U2 pad 16: (no net) -> lv
- U2 pad 17: (no net) -> lv
- U2 pad 18: (no net) -> lv
- U2 pad 19: (no net) -> lv
- U2 pad 20: (no net) -> lv
- U20 pad 3: (no net) -> lv
- U200 pad 3: (no net) -> lv
- U201 pad 3: (no net) -> lv
- U202 pad 3: (no net) -> lv
- U203 pad 3: (no net) -> lv
- U204 pad 3: (no net) -> lv
- U205 pad 3: (no net) -> lv
- U206 pad 12: (no net) -> lv
- U206 pad 15: (no net) -> lv
- U206 pad 16: (no net) -> lv
- U206 pad 17: (no net) -> lv
- U206 pad 18: (no net) -> lv
- U206 pad 19: (no net) -> lv
- U206 pad 20: (no net) -> lv
- U207 pad 3: (no net) -> lv
- U208 pad 3: (no net) -> lv
- U209 pad 3: (no net) -> lv
- U21 pad 3: (no net) -> lv
- U210 pad 3: (no net) -> lv
- U211 pad 3: (no net) -> lv
- U212 pad 3: (no net) -> lv
- U213 pad 3: (no net) -> lv
- U214 pad 3: (no net) -> lv
- U215 pad 3: (no net) -> lv
- U216 pad 3: (no net) -> lv
- U217 pad 3: (no net) -> lv
- U218 pad 12: (no net) -> lv
- U218 pad 15: (no net) -> lv
- U218 pad 16: (no net) -> lv
- U218 pad 17: (no net) -> lv
- U218 pad 18: (no net) -> lv
- U218 pad 19: (no net) -> lv
- U218 pad 20: (no net) -> lv
- U219 pad 3: (no net) -> lv
- U22 pad 3: (no net) -> lv
- U220 pad 3: (no net) -> lv
- U221 pad 3: (no net) -> lv
- U222 pad 3: (no net) -> lv
- U223 pad 3: (no net) -> lv
- U224 pad 3: (no net) -> lv
- U225 pad 3: (no net) -> lv
- U226 pad 3: (no net) -> lv
- U227 pad 3: (no net) -> lv
- U228 pad 3: (no net) -> lv
- U229 pad 3: (no net) -> lv
- U23 pad 3: (no net) -> lv
- U24 pad 3: (no net) -> lv
- U25 pad 3: (no net) -> lv
- U26 pad 12: (no net) -> lv
- U26 pad 15: (no net) -> lv
- U26 pad 16: (no net) -> lv
- U26 pad 17: (no net) -> lv
- U26 pad 18: (no net) -> lv
- U26 pad 19: (no net) -> lv
- U26 pad 20: (no net) -> lv
- U27 pad 3: (no net) -> lv
- U28 pad 3: (no net) -> lv
- U29 pad 3: (no net) -> lv
- U3 pad 3: (no net) -> lv
- U30 pad 3: (no net) -> lv
- U31 pad 3: (no net) -> lv
- U32 pad 3: (no net) -> lv
- U33 pad 3: (no net) -> lv
- U34 pad 3: (no net) -> lv
- U35 pad 3: (no net) -> lv
- U36 pad 3: (no net) -> lv
- U37 pad 3: (no net) -> lv
- U38 pad 12: (no net) -> lv
- U38 pad 15: (no net) -> lv
- U38 pad 16: (no net) -> lv
- U38 pad 17: (no net) -> lv
- U38 pad 18: (no net) -> lv
- U38 pad 19: (no net) -> lv
- U38 pad 20: (no net) -> lv
- U39 pad 3: (no net) -> lv
- U4 pad 3: (no net) -> lv
- U40 pad 3: (no net) -> lv
- U41 pad 3: (no net) -> lv
- U42 pad 3: (no net) -> lv
- U43 pad 3: (no net) -> lv
- U44 pad 3: (no net) -> lv
- U45 pad 3: (no net) -> lv
- U46 pad 3: (no net) -> lv
- U47 pad 3: (no net) -> lv
- U48 pad 3: (no net) -> lv
- U49 pad 3: (no net) -> lv
- U5 pad 3: (no net) -> lv
- U50 pad 12: (no net) -> lv
- U50 pad 15: (no net) -> lv
- U50 pad 16: (no net) -> lv
- U50 pad 17: (no net) -> lv
- U50 pad 18: (no net) -> lv
- U50 pad 19: (no net) -> lv
- U50 pad 20: (no net) -> lv
- U51 pad 3: (no net) -> lv
- U52 pad 3: (no net) -> lv
- U53 pad 3: (no net) -> lv
- U54 pad 3: (no net) -> lv
- U55 pad 3: (no net) -> lv
- U56 pad 3: (no net) -> lv
- U57 pad 3: (no net) -> lv
- U58 pad 3: (no net) -> lv
- U59 pad 3: (no net) -> lv
- U6 pad 3: (no net) -> lv
- U60 pad 3: (no net) -> lv
- U61 pad 3: (no net) -> lv
- U62 pad 12: (no net) -> lv
- U62 pad 15: (no net) -> lv
- U62 pad 16: (no net) -> lv
- U62 pad 17: (no net) -> lv
- U62 pad 18: (no net) -> lv
- U62 pad 19: (no net) -> lv
- U62 pad 20: (no net) -> lv
- U63 pad 3: (no net) -> lv
- U64 pad 3: (no net) -> lv
- U65 pad 3: (no net) -> lv
- U66 pad 3: (no net) -> lv
- U67 pad 3: (no net) -> lv
- U68 pad 3: (no net) -> lv
- U69 pad 3: (no net) -> lv
- U7 pad 3: (no net) -> lv
- U70 pad 3: (no net) -> lv
- U71 pad 3: (no net) -> lv
- U72 pad 3: (no net) -> lv
- U73 pad 3: (no net) -> lv
- U74 pad 12: (no net) -> lv
- U74 pad 15: (no net) -> lv
- U74 pad 16: (no net) -> lv
- U74 pad 17: (no net) -> lv
- U74 pad 18: (no net) -> lv
- U74 pad 19: (no net) -> lv
- U74 pad 20: (no net) -> lv
- U75 pad 3: (no net) -> lv
- U76 pad 3: (no net) -> lv
- U77 pad 3: (no net) -> lv
- U78 pad 3: (no net) -> lv
- U79 pad 3: (no net) -> lv
- U8 pad 3: (no net) -> lv
- U80 pad 3: (no net) -> lv
- U81 pad 3: (no net) -> lv
- U82 pad 3: (no net) -> lv
- U83 pad 3: (no net) -> lv
- U84 pad 3: (no net) -> lv
- U85 pad 3: (no net) -> lv
- U86 pad 12: (no net) -> lv
- U86 pad 15: (no net) -> lv
- U86 pad 16: (no net) -> lv
- U86 pad 17: (no net) -> lv
- U86 pad 18: (no net) -> lv
- U86 pad 19: (no net) -> lv
- U86 pad 20: (no net) -> lv
- U87 pad 3: (no net) -> lv
- U88 pad 3: (no net) -> lv
- U89 pad 3: (no net) -> lv
- U9 pad 3: (no net) -> lv
- U90 pad 3: (no net) -> lv
- U91 pad 3: (no net) -> lv
- U92 pad 3: (no net) -> lv
- U93 pad 3: (no net) -> lv
- U94 pad 3: (no net) -> lv
- U95 pad 3: (no net) -> lv
- U96 pad 3: (no net) -> lv
- U97 pad 3: (no net) -> lv
- U98 pad 12: (no net) -> lv
- U98 pad 15: (no net) -> lv
- U98 pad 16: (no net) -> lv
- U98 pad 17: (no net) -> lv
- U98 pad 18: (no net) -> lv
- U98 pad 19: (no net) -> lv
- U98 pad 20: (no net) -> lv
- U99 pad 3: (no net) -> lv
- X1 pad 2: (no net) -> lv
- X1 pad 4: (no net) -> lv

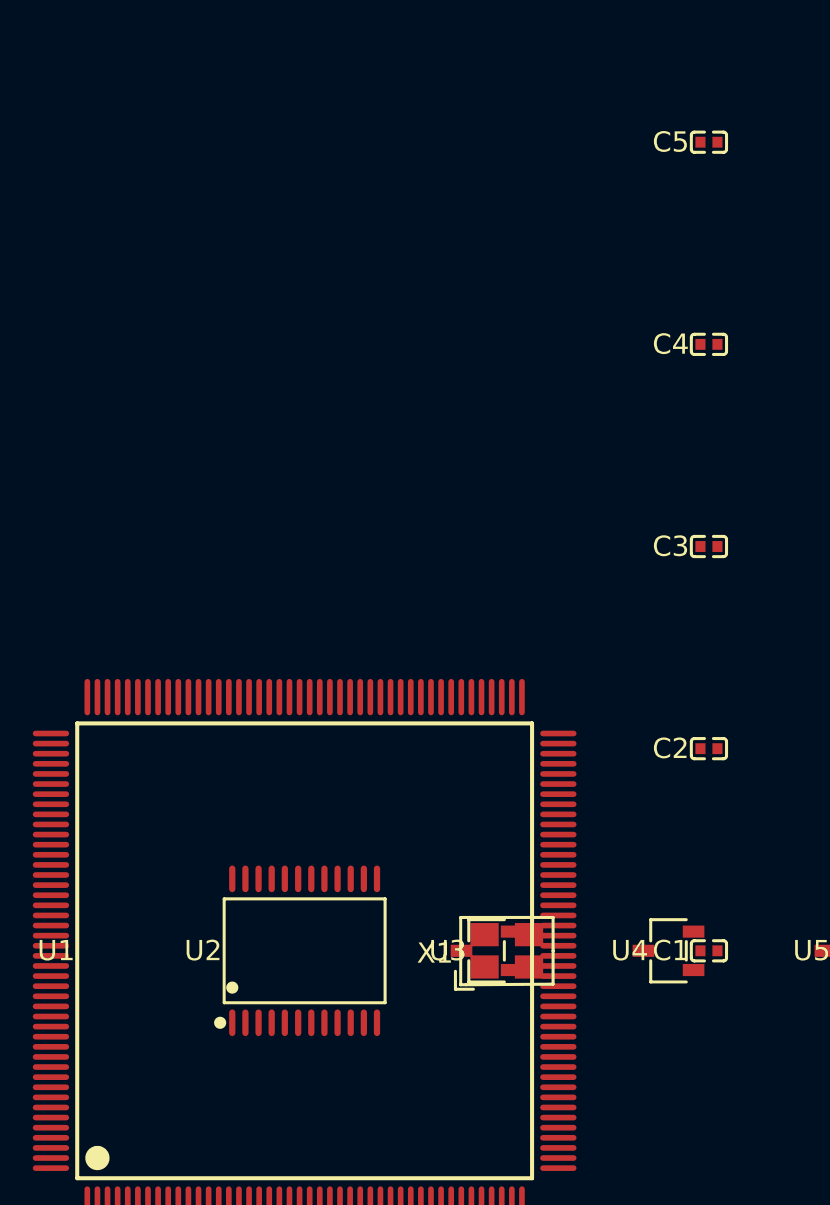
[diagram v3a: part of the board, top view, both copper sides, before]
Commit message: pcb: add buck converter
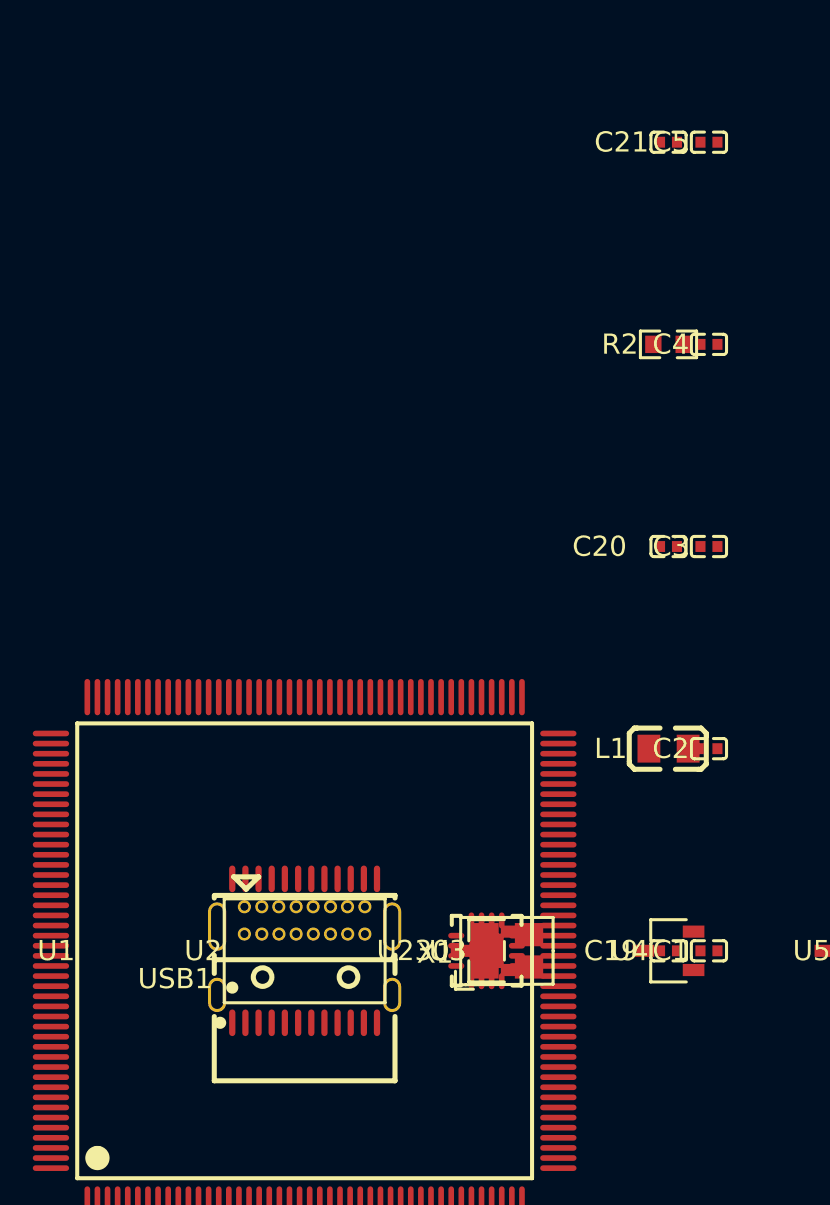
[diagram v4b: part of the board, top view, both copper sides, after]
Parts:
- added C19: 10µF ±20%, Samsung_Electro_Mechanics_CL05A106MP5NUNC:C0402, F.Cu at (18.0, 0.00)
- added C20: 22µF ±20%, HRE_CGA0402X5R226M100GT:C0402, F.Cu at (18.0, -20.0)
- added C21: 3.3nF ±10%, YAGEO_CC0402KRX7R9BB332:C0402, F.Cu at (18.0, -40.0)
- added L1: L 2.2µH ±10%, FH_CMI201209U2R2KT:L0805, F.Cu at (18.0, -10.0)
- added R2: 100kΩ ±1%, UNI_ROYAL_0603WAF1003T5E:R0603, F.Cu at (18.0, -30.0)
- added U230: , Texas_Instruments_TPS62152RGTR:TQFN-16_L3.0-W3.0-P0.50-TL-EP1.7, F.Cu at (9.00, 0.00)
- added USB1: , GCT_USB4085_GF_A:USC-C-SMD_USB4085-GF-A, F.Cu at (0.00, 0.00)
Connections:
- net hv renamed vref_caps[1]-power-hv
